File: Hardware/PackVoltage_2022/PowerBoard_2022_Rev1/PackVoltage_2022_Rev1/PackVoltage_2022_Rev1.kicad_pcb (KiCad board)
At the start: 2 copper layers, 115 parts, among them Q1 BUK7M8R0-40EX, Q2 BUK7M8R0-40EX, Q3 BUK7M8R0-40EX, Q4 BUK7M8R0-40EX, Q5 BUK7M8R0-40EX, Q6 BUK7M8R0-40EX, Q7 BUK7M8R0-40EX, Q8 BUK7M8R0-40EX, U1 OKI, U10 INA281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

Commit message: Organizing stuff
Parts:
- removed Conn1: Molex_SL_10, MRDT_Connectors:MOLEX_SL_10_Vertical
- removed Conn2: Molex_SL_02, MRDT_Connectors:MOLEX_SL_02_Vertical
- Q1, Q2, Q3, Q4, Q5, Q6, Q7, Q8: value BUK7M8R0-40EX -> BUK7S2R0-40HJ
- U19: value TM4C129E_Launchpad -> Teensy4.1_DEV-16771; footprint MRDT_Shields:TM4C129E_Launchpad_FULL_THT_TOP -> MRDT_Shields:MODULE_DEV-16771
- moved Conn6 285.2 mm to (628.9, 38.0)
- moved Conn11 218.5 mm to (592.9, 85.3)
- moved Conn9 208.1 mm to (628.6, 84.5)
- moved Conn5 206.9 mm to (597.8, 40.5)
- moved Conn4 186.5 mm to (564.1, 39.1)
- moved Conn8 160.6 mm to (560.5, 84.2)
- moved Conn7 148.3 mm to (526.6, 84.4)
- moved Conn3 137.7 mm to (528.3, 38.4)
- moved C7 135.5 mm to (305.6, 81.5)
- moved R24 123.5 mm to (630.2, 95.6)
- moved C8 118.1 mm to (320.3, 81.8)
- moved Conn10 112.3 mm to (476.0, 76.8)
- moved F4 111.5 mm to (620.4, 28.4), turned to 270 degrees
- moved C10 101.4 mm to (354.6, 81.5)
- moved U1 101.2 mm to (452.4, 113.7)
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
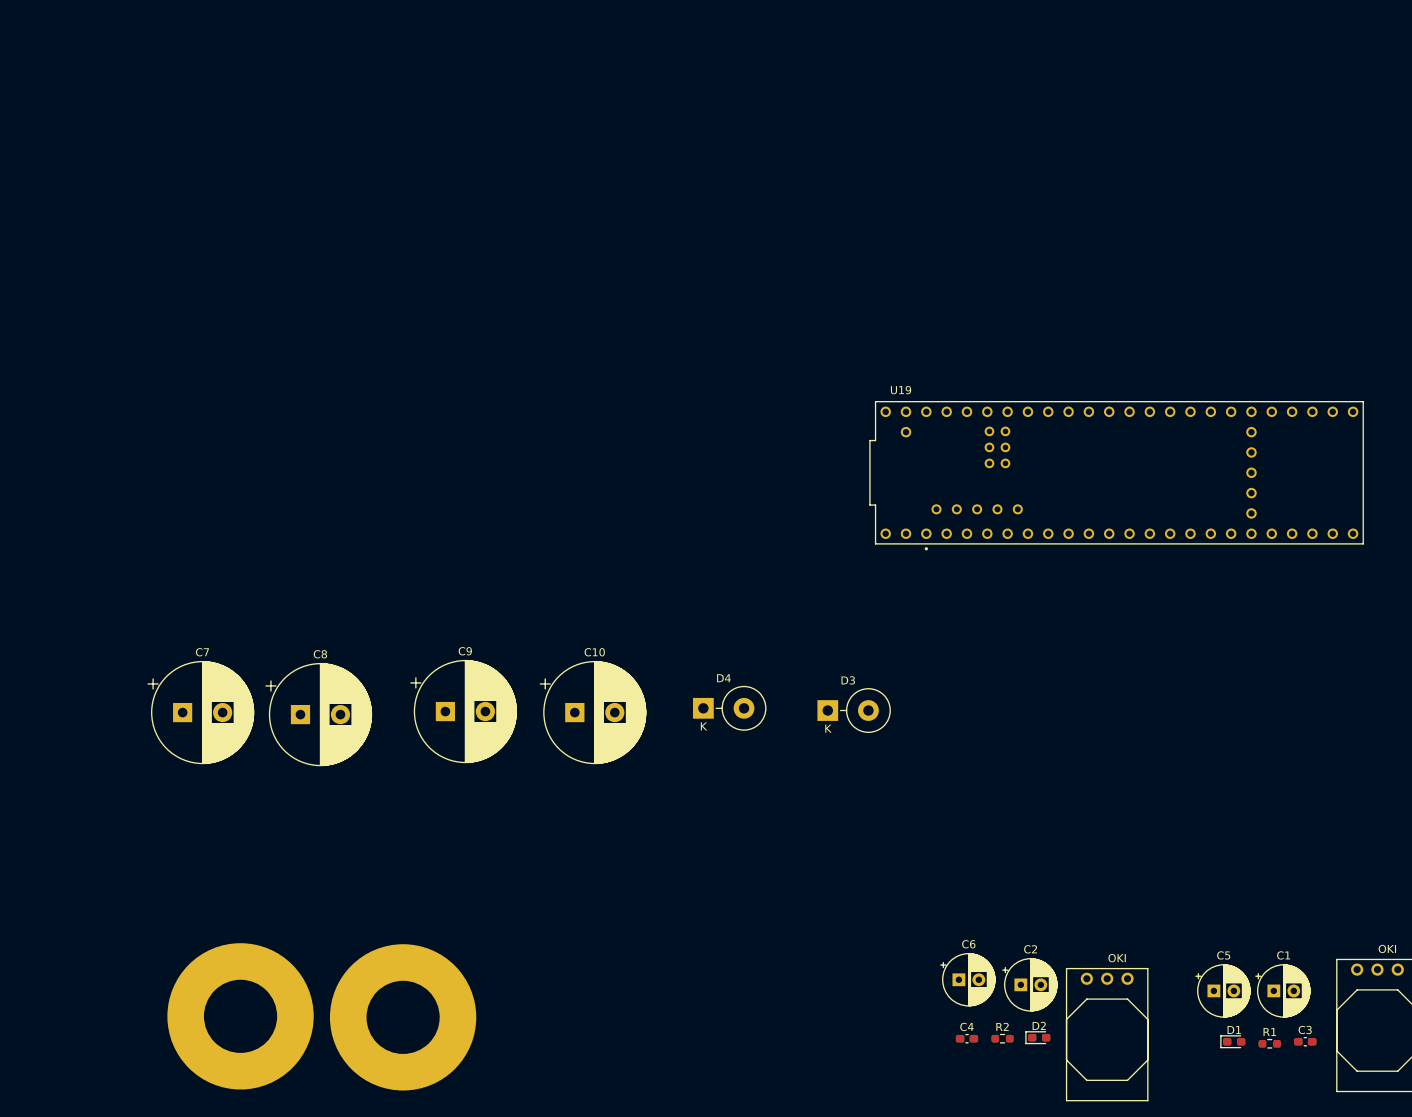
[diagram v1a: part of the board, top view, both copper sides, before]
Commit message: added molex footprints to layout + saving.
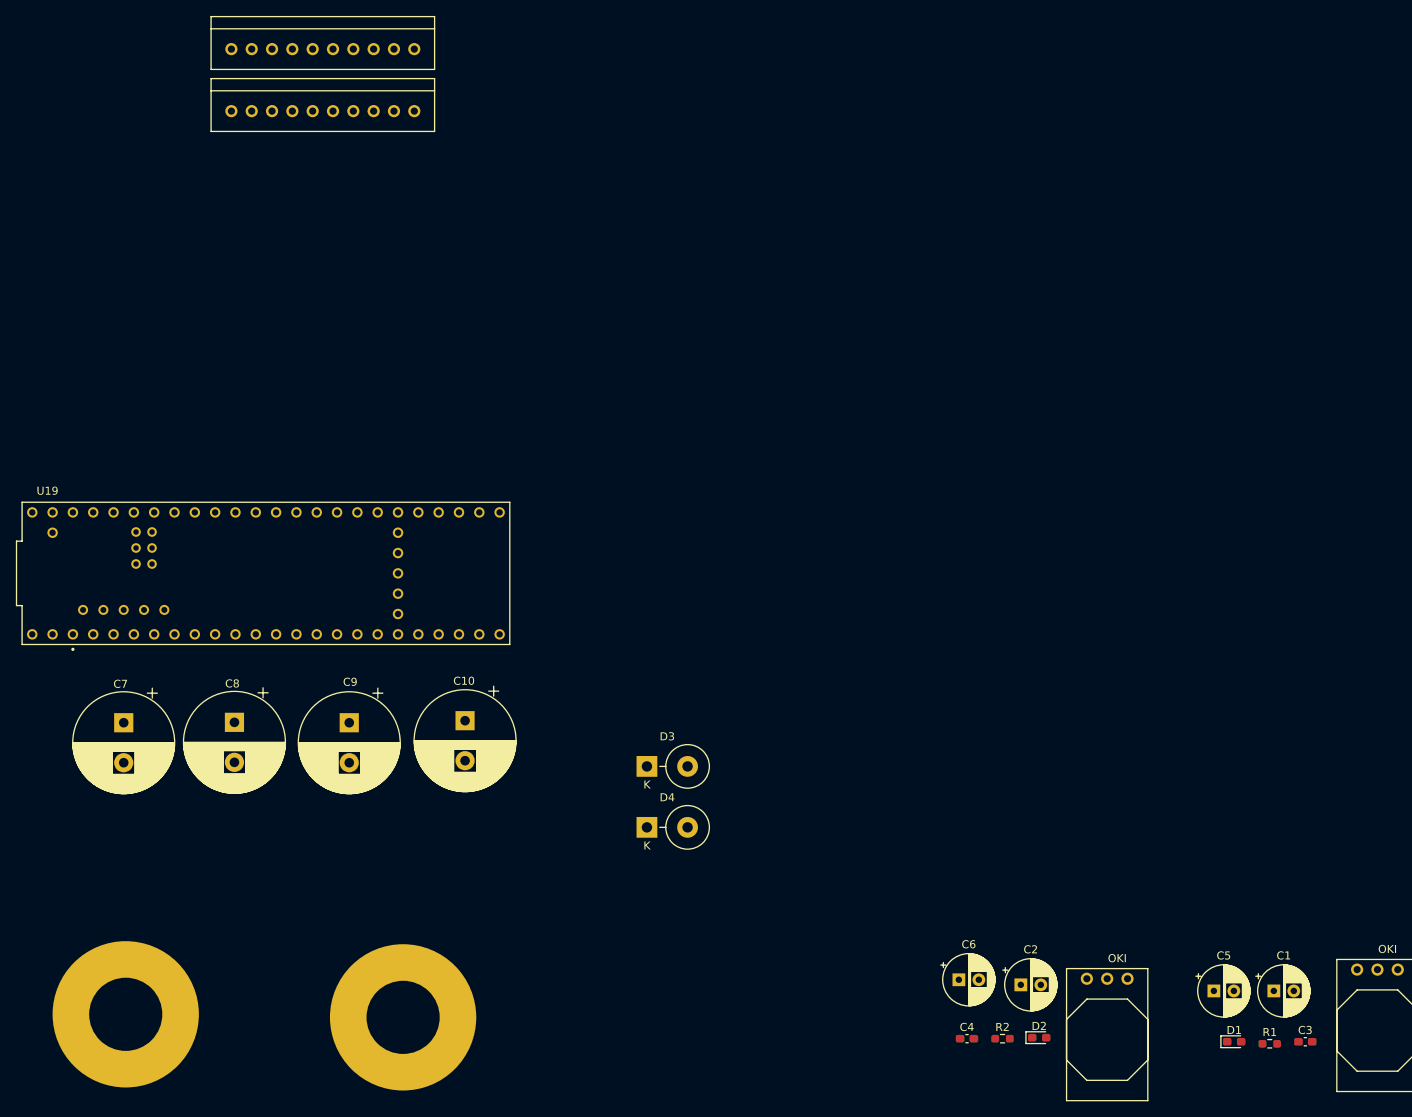
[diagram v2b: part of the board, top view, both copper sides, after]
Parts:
- added Conn1: Molex_SL_10, MRDT_Connectors:MOLEX_SL_10_Vertical, F.Cu at (311.7, -1.40)
- added Conn2: Molex_SL_10, MRDT_Connectors:MOLEX_SL_10_Vertical, F.Cu at (311.7, 6.35)
- moved U19 107.4 mm to (316.0, 64.1)
- moved D3 23.7 mm to (363.6, 88.3)
- moved D4 16.5 mm to (363.6, 95.9)
- moved GND1 14.4 mm to (298.4, 119.3)
- moved C10 13.8 mm to (340.9, 82.5), turned to 270 degrees
- moved C9 12.1 mm to (326.4, 82.8), turned to 270 degrees
- moved C8 8.31 mm to (312.0, 82.8), turned to 270 degrees
- moved C7 7.47 mm to (298.2, 82.8), turned to 270 degrees
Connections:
- U19 pad 11: Net-(U19-Pad11) -> Driver_GimLog
- U19 pad 12: Net-(U19-Pad12) -> Driver_GimAct
- U19 pad 13: Net-(U19-Pad13) -> Driver_Multi
- U19 pad 22: Net-(U19-Pad22) -> Current_Sensor_AuxLog
- U19 pad 23: Net-(U19-Pad23) -> Current_Sensor_NetSwitch
- U19 pad 24: Net-(U19-Pad24) -> Current_Sensor_Nav
- U19 pad 25: Net-(U19-Pad25) -> Current_Sensor_Multi
- U19 pad 26: Net-(U19-Pad26) -> Current_Sensor_GimLog
- U19 pad 27: Net-(U19-Pad27) -> Current_Sensor_GimAct
- U19 pad 3: Net-(U19-Pad3) -> Driver_AuxLog
- U19 pad 30: Net-(U19-Pad30) -> Driver_Cam1
- U19 pad 31: Net-(U19-Pad31) -> Driver_Cam2
- U19 pad 33: Net-(U19-Pad33) -> Driver_Drive
- U19 pad 36: Net-(U19-Pad36) -> Driver_NetSwitch
- U19 pad 37: Net-(U19-Pad37) -> Driver_Nav
- U19 pad 38: Net-(U19-Pad38) -> Current_Sensor_Drive
- U19 pad 39: Net-(U19-Pad39) -> Current_Sensor_Cam2
- U19 pad 4: Net-(U19-Pad4) -> Driver_BBB
- U19 pad 40: Net-(U19-Pad40) -> Current_Sensor_Cam1
- U19 pad 41: Net-(U19-Pad41) -> Current_Sensor_BBB

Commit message: Organized the board and started placing components in their locations
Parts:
- added C27: 0.1 uF, Capacitor_SMD:C_0603_1608Metric_Pad1.08x0.95mm_HandSolder, F.Cu at (145.5, 51.3)
- added Conn12: Molex_uF_D_06, MRDT_Connectors:MOLEX_uF_D_06_Horizontal, F.Cu at (151.9, 55.1)
- added J1: RJ45_LED_Shielded, MRDT_Connectors:RJ45_Teensy, F.Cu at (151.4, 22.1)
- R1: value 510 -> 300
- R2: value 330 -> 100
- moved F1 397.5 mm to (137.2, 139.2), turned to 90 degrees
- moved U7 396.2 mm to (136.2, 100.9), turned to 90 degrees
- moved R9 396.0 mm to (141.5, 102.6), turned to 90 degrees
- moved U3 392.7 mm to (137.9, 117.1)
- moved Conn3 391.4 mm to (139.7, 85.3), turned to 270 degrees
- moved R3 391.1 mm to (132.3, 119.8), turned to 270 degrees
- moved C15 390.7 mm to (133.0, 126.7), turned to 180 degrees
- moved C11 390.2 mm to (132.3, 115.5), turned to 90 degrees
- moved Q1 388.3 mm to (138.8, 110.7)
- moved D5 386.8 mm to (133.1, 108.6), turned to 90 degrees
- moved R7 384.1 mm to (135.9, 105.7)
- moved R15 368.8 mm to (116.9, 111.2), turned to 180 degrees
- moved F5 363.2 mm to (114.8, 125.7), turned to 270 degrees
- moved Conn10 362.6 mm to (113.5, 85.3), turned to 270 degrees
- moved C1 361.0 mm to (91.3, 30.5), turned to 180 degrees
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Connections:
- net Current_Sensor_GimLog renamed Current_Sensor_Gim
- net Driver_GimLog renamed Driver_Gim
- Conn1 pad 2: Driver_BBB -> Driver_AuxAct
- Conn1 pad 3: Driver_Cam1 -> Driver_BBB
- Conn1 pad 4: Driver_Cam2 -> Driver_Cam1
- Conn1 pad 5: Driver_Drive -> Driver_Cam2
- Conn1 pad 6: Driver_GimAct -> Driver_Drive
- Conn2 pad 2: Current_Sensor_BBB -> Current_Sensor_AuxAct
- Conn2 pad 3: Current_Sensor_Cam1 -> Current_Sensor_BBB
- Conn2 pad 4: Current_Sensor_Cam2 -> Current_Sensor_Cam1
- Conn2 pad 5: Current_Sensor_Drive -> Current_Sensor_Cam2
- Conn2 pad 6: Current_Sensor_GimAct -> Current_Sensor_Drive
- U19 pad 10: Net-(U19-Pad10) -> Driver_AuxAct
- U19 pad 12: Driver_GimAct -> Net-(U19-Pad12)
- U19 pad 27: Current_Sensor_GimAct -> Current_Sensor_Drive
- U19 pad 38: Current_Sensor_Drive -> Current_Sensor_Cam2
- U19 pad 39: Current_Sensor_Cam2 -> Current_Sensor_Cam1
- U19 pad 40: Current_Sensor_Cam1 -> Current_Sensor_BBB
- U19 pad 41: Current_Sensor_BBB -> Current_Sensor_AuxLog
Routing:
- added copper zone on F.Cu, net GND
- added copper zone on B.Cu, net PV
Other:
- board outline added: 177.8 x 127 mm

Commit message: Wired a few circuits, mainly oki and ethernet and M1
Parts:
- moved R7 1.93 mm to (134.0, 105.7)
- moved D5 1.02 mm to (133.1, 109.6)
- moved C3 0.15 mm to (129.6, 54.4)
- moved R1 0.10 mm to (129.7, 57.9)
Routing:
- net +5V: track 0.00 -> 41.0 mm, vias 0 -> 3
- net Net-(C27-Pad2): track 0.00 -> 38.3 mm
- net Driver_M1: track 0.00 -> 31.3 mm, vias 0 -> 2
- net Net-(Conn12-Pad4): track 0.00 -> 27.3 mm
- net Net-(C27-Pad1): track 0.00 -> 20.7 mm
- net Net-(Conn12-Pad1): track 0.00 -> 19.3 mm, vias 0 -> 2
- net Net-(Conn12-Pad2): track 0.00 -> 17.6 mm
- net +3V3: track 0.00 -> 14.7 mm
- net Net-(Conn12-Pad6): track 0.00 -> 12.7 mm
- net Net-(Conn12-Pad5): track 0.00 -> 12.3 mm, vias 0 -> 2
- net Net-(Q1-Pad4): track 0.00 -> 9.13 mm
- net Current_Sensor_M1: track 0.00 -> 7.00 mm
- net Net-(R3-Pad1): track 0.00 -> 3.52 mm
- net Net-(Q1-Pad1): track 0.00 -> 3.13 mm
- net Net-(C11-Pad1): track 0.00 -> 3.10 mm
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- added copper zone on F.Cu, net /MOTORS/Anderson_M1
- added copper zone on F.Cu, net Net-(C15-Pad1)
- added copper zone on F.Cu, net Net-(Q1-Pad1)

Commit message: Added all the components to the board and began wiring them together
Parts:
- added REF**: 4_40_Hole, MRDT_Drill_Holes:4_40_Hole_Corner, F.Cu at (72.0, 143.1)
- added REF**: 4_40_Hole, MRDT_Drill_Holes:4_40_Hole_Corner, F.Cu at (72.0, 32.1)
- added REF**: 4_40_Hole, MRDT_Drill_Holes:4_40_Hole_Corner, F.Cu at (233.8, 143.1)
- added REF**: 4_40_Hole, MRDT_Drill_Holes:4_40_Hole_Corner, F.Cu at (233.8, 32.1)
- moved U16 471.2 mm to (228.2, 99.8), turned to 90 degrees
- moved Conn9 470.7 mm to (231.9, 84.3), turned to 270 degrees
- moved R24 470.5 mm to (233.7, 101.3), turned to 90 degrees
- moved F7 469.7 mm to (229.1, 138.2), turned to 90 degrees
- moved U12 464.8 mm to (230.3, 116.0)
- moved C24 463.2 mm to (225.3, 126.1), turned to 180 degrees
- moved R17 463.2 mm to (224.7, 118.8), turned to 270 degrees
- moved C20 463.0 mm to (224.7, 114.5), turned to 90 degrees
- moved Q6 462.6 mm to (231.0, 109.7)
- moved D11 462.1 mm to (225.6, 108.5), turned to 90 degrees
- moved R21 461.4 mm to (226.4, 104.7)
- moved F9 442.1 mm to (197.7, 138.1), turned to 90 degrees
- moved U15 431.4 mm to (212.5, 99.8), turned to 90 degrees
- moved R23 431.1 mm to (217.8, 101.4), turned to 90 degrees
- moved Conn11 431.0 mm to (216.3, 84.3), turned to 270 degrees
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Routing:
- net +5V: track 41.0 -> 309.0 mm, vias 3 -> 24
- net Driver_Spare: track 0.00 -> 31.7 mm, vias 0 -> 2
- net Driver_POE: track 0.00 -> 31.6 mm, vias 0 -> 2
- net Driver_M3: track 0.00 -> 31.4 mm, vias 0 -> 2
- net Driver_M6: track 0.00 -> 31.3 mm, vias 0 -> 2
- net Driver_M2: track 0.00 -> 31.1 mm, vias 0 -> 2
- net Driver_M5: track 0.00 -> 31.0 mm, vias 0 -> 2
- net Driver_M4: track 0.00 -> 30.9 mm, vias 0 -> 2
- net Net-(Q7-Pad4): track 0.00 -> 9.23 mm
- net Net-(Q3-Pad4): track 0.00 -> 9.20 mm
- net Net-(Q4-Pad4): track 0.00 -> 9.20 mm
- net Net-(Q6-Pad4): track 0.00 -> 9.16 mm
- net Net-(Q5-Pad4): track 0.00 -> 9.16 mm
- net Net-(Q2-Pad4): track 0.00 -> 9.15 mm
- net Net-(Q8-Pad4): track 0.00 -> 9.08 mm
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- added copper zone on F.Cu, net (none)
- added copper zone on F.Cu, net /MOTORS/12V
- added copper zone on F.Cu, net /MOTORS/Anderson_M2
- added copper zone on F.Cu, net /MOTORS/Anderson_M3
- added copper zone on F.Cu, net /MOTORS/Anderson_M4
- added copper zone on F.Cu, net /MOTORS/Anderson_M5
- added copper zone on F.Cu, net /MOTORS/Anderson_POE
- added copper zone on F.Cu, net /MOTORS/Anderson_Spare
- added copper zone on F.Cu, net Net-(C16-Pad1)
- added copper zone on F.Cu, net Net-(C17-Pad1)
- added copper zone on F.Cu, net Net-(C18-Pad1)
- added copper zone on F.Cu, net Net-(C23-Pad1)
- added copper zone on F.Cu, net Net-(C24-Pad1)
- added copper zone on F.Cu, net Net-(C25-Pad1)
- added copper zone on F.Cu, net Net-(C26-Pad1)
- added copper zone on F.Cu, net Net-(Q2-Pad1)
- added copper zone on F.Cu, net Net-(Q3-Pad1)
- added copper zone on F.Cu, net Net-(Q4-Pad1)
- added copper zone on F.Cu, net Net-(Q5-Pad1)
- added copper zone on F.Cu, net Net-(Q6-Pad1)
- added copper zone on F.Cu, net Net-(Q7-Pad1)
- added copper zone on F.Cu, net Net-(Q8-Pad1)
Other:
- outline, holes or cut-outs redrawn
- board text added: "Pack Power Board "Baker's Dozen" Designed by Dakota Miller, Josh Perkins, and Nithin Vijay"

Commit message: wiring smile :), I'll finish after chapter.
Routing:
- net Current_Sensor_Nav: track 0.00 -> 101.5 mm, vias 0 -> 2
- net Current_Sensor_Multi: track 0.00 -> 99.4 mm, vias 0 -> 2
- net Current_Sensor_Gim: track 0.00 -> 97.7 mm, vias 0 -> 2
- net Current_Sensor_Drive: track 0.00 -> 95.4 mm, vias 0 -> 2
- net Current_Sensor_NetSwitch: track 0.00 -> 63.4 mm, vias 0 -> 2
- net Current_Sensor_Cam2: track 0.00 -> 20.4 mm
- net Current_Sensor_Cam1: track 0.00 -> 20.4 mm
- net Current_Sensor_BBB: track 0.00 -> 20.4 mm

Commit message: more wiring
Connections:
- U19 pad 41: Current_Sensor_AuxLog -> Current_Sensor_AuxAct
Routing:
- net Driver_AuxLog: track 0.00 -> 151.4 mm, vias 0 -> 4
- net Current_Sensor_Spare: track 6.75 -> 154.6 mm, vias 0 -> 2
- net Driver_BBB: track 0.00 -> 141.5 mm, vias 0 -> 2
- net Driver_Gim: track 0.00 -> 137.5 mm, vias 0 -> 2
- net Driver_AuxAct: track 0.00 -> 126.9 mm, vias 0 -> 2
- net Current_Sensor_M6: track 6.91 -> 111.0 mm, vias 0 -> 6
- net Current_Sensor_POE: track 6.78 -> 108.9 mm, vias 0 -> 4
- net Driver_POE: track 31.6 -> 133.2 mm
- net Driver_Cam1: track 0.00 -> 100.2 mm, vias 0 -> 2
- net Driver_Cam2: track 0.00 -> 96.6 mm, vias 0 -> 2
- net Driver_Spare: track 31.7 -> 127.7 mm, vias 2 -> 4
- net Driver_M6: track 31.3 -> 92.6 mm
- net Driver_Drive: track 0.00 -> 57.8 mm, vias 0 -> 2
- net Driver_NetSwitch: track 0.00 -> 45.3 mm, vias 0 -> 2
- net Driver_Nav: track 0.00 -> 44.4 mm, vias 0 -> 2
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
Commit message: wiring finished
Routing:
- net Current_Sensor_M1: track 6.59 -> 177.7 mm, vias 0 -> 6
- net Current_Sensor_M2: track 21.9 -> 164.4 mm, vias 0 -> 4
- net Current_Sensor_M5: track 22.4 -> 163.1 mm, vias 0 -> 6
- net Current_Sensor_M4: track 22.4 -> 144.3 mm, vias 0 -> 6
- net Current_Sensor_M3: track 21.9 -> 127.1 mm, vias 0 -> 6
- net Driver_M2: track 46.3 -> 107.7 mm, vias 2 -> 4
- net Driver_M3: track 47.0 -> 108.3 mm, vias 2 -> 4
- net Driver_M1: track 47.2 -> 108.5 mm, vias 2 -> 6
- net Driver_M5: track 46.2 -> 104.2 mm, vias 2 -> 6
- net Driver_M4: track 46.1 -> 95.2 mm, vias 2 -> 4
